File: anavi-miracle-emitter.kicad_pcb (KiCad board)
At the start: 2 copper layers, 57.7 x 47.2 mm, 19 parts, among them J1 Conn_01x04_Female, J2 Conn_01x04_Female, J3 Conn_01x04_Female, J4 Conn_01x04_Female, J5 Conn_01x04_Male, J6 Conn_01x05_Male, J7 Screw_Terminal_01x03, U1 MOUDLE-SEEEDUINO-XIAO-ESP32C3, U2 74LVC1G17W5-7

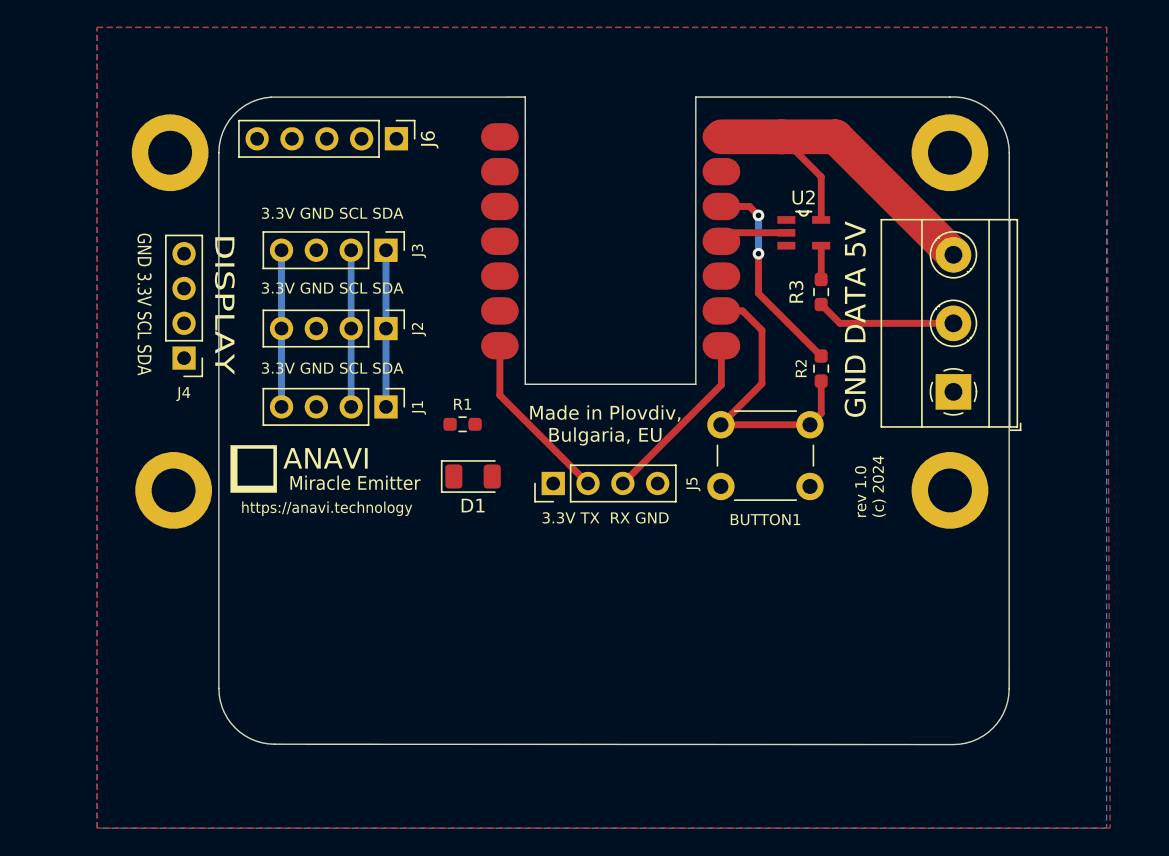
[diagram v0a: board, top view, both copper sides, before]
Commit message: Update PCB
Update PCB routing and edge cuts.

Signed-off-by: Leon Anavi <leon@anavi.org>
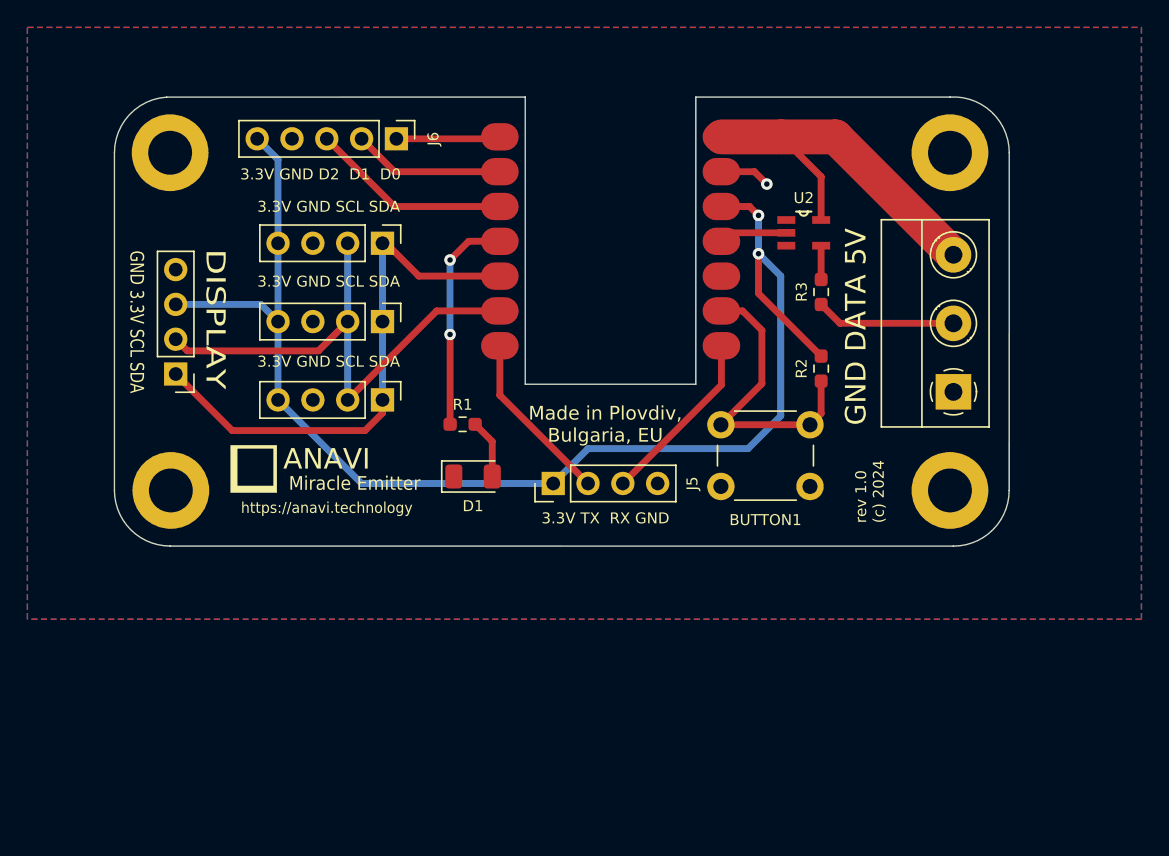
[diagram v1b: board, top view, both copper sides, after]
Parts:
- D1: value LED -> KP-3216EC
- moved J4 1.31 mm to (117.5, 53.2)
- moved J2 0.57 mm to (132.6, 49.4)
- moved J1 0.57 mm to (132.6, 55.1)
- moved J3 0.57 mm to (132.6, 43.7)
- moved REF** 0.20 mm to (117.1, 61.7)
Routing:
- net +3V3: track 27.0 -> 96.6 mm
- net Net-(J1-Pad1): track 11.4 -> 39.3 mm
- net Net-(J1-Pad2): track 11.4 -> 39.0 mm
- net Net-(R1-Pad1): track 0.00 -> 16.2 mm, vias 0 -> 2
- net Net-(J6-Pad3): track 0.00 -> 14.7 mm
- net Net-(J6-Pad2): track 0.00 -> 11.1 mm
- net Net-(J6-Pad1): track 0.00 -> 7.60 mm
- net Net-(D1-Pad2): track 0.00 -> 4.33 mm
- net GND: track 0.00 -> 3.69 mm, vias 0 -> 1
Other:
- board size 57.7 x 47.2 mm -> 65.3 x 32.8 mm
- board text added: "3.3V GND D2 D1 D0"
- board text removed: ":)"
- board text removed: "Plug your plants into the digital conversation!"
